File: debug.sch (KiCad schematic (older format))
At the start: 47 parts, among them J1 ZX62D-AB-5P8, P1 LPC-Link, P2 UART, P3 JTAG, P4 Cortex-Debug, P5 Vout, U1 93C46, U2 PRTR5V0U2X, U3 FT2232H, U4 LD1117S33CTR, X1 12MHz

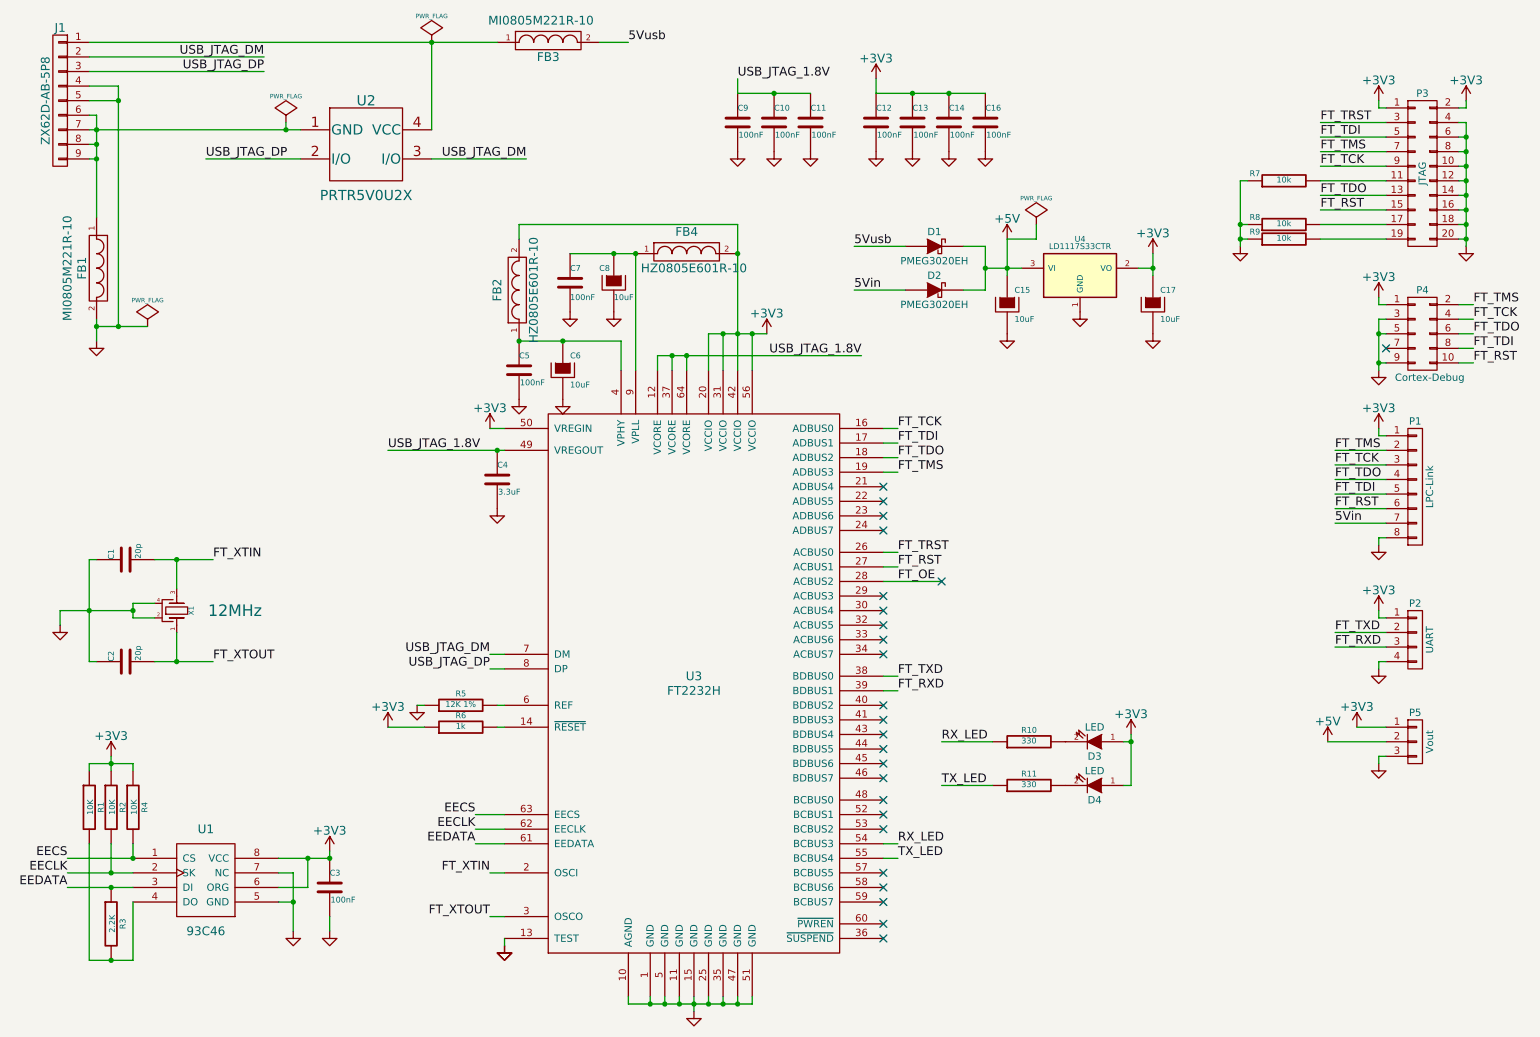
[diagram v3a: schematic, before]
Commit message: pcb terminado, enviado a fabricacion
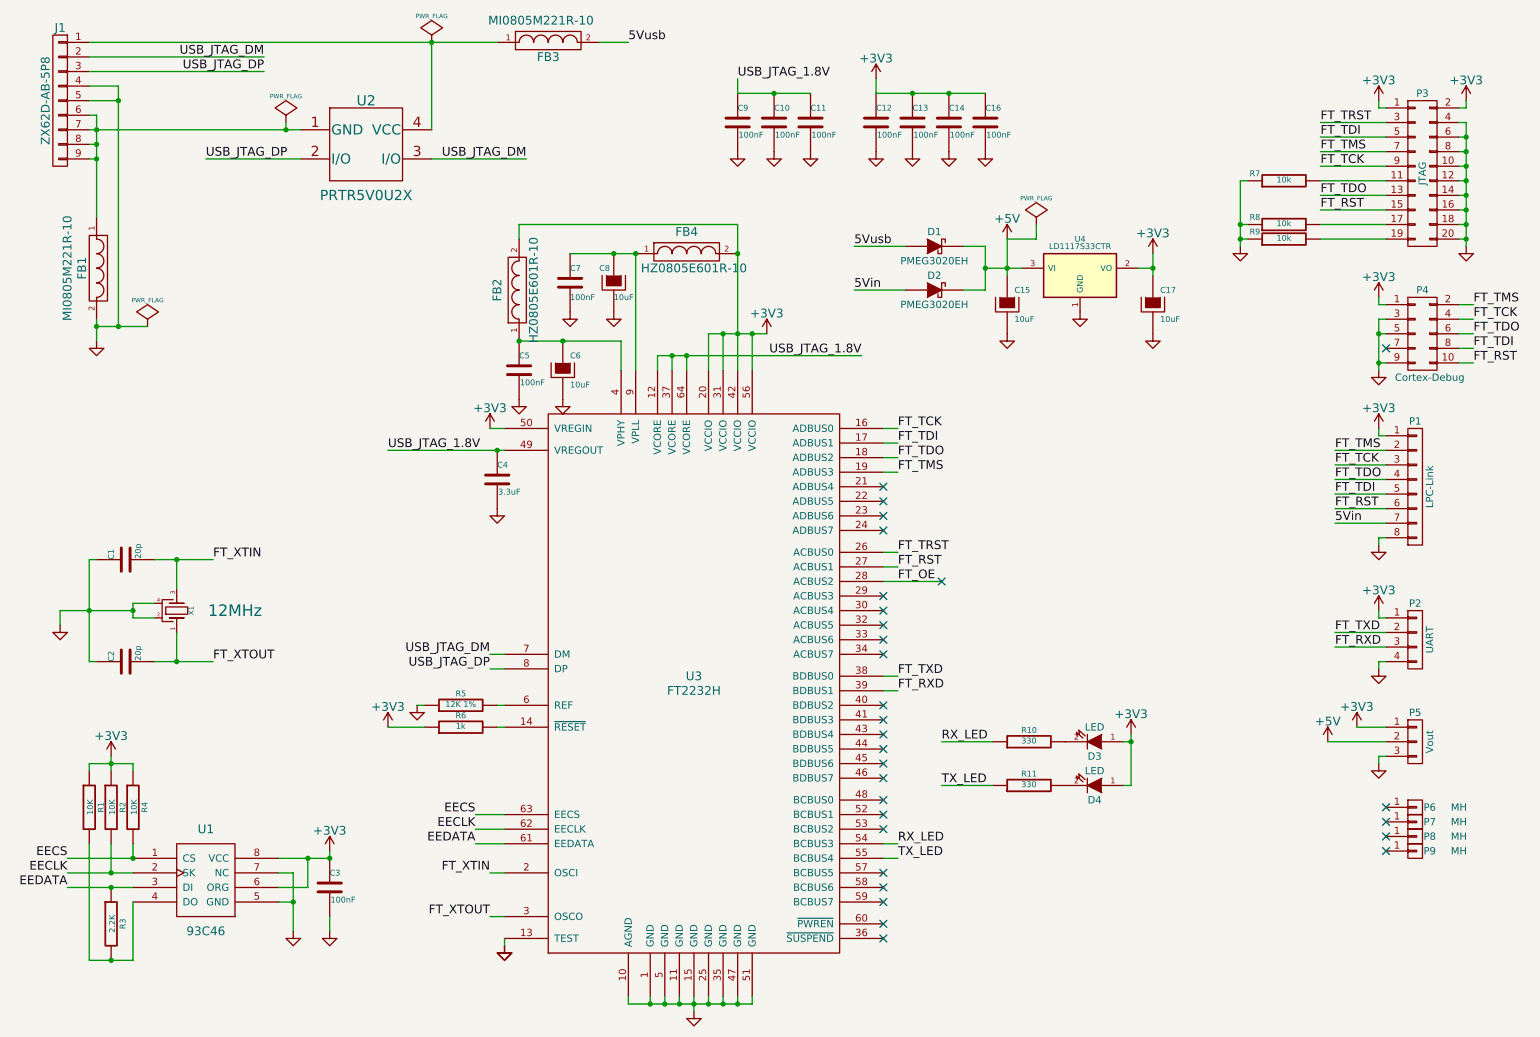
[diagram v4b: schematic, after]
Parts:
- added P6, P7, P8, P9: MH, Connect:1pin, symbol CONN_01X01
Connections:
- no-connect marks 25 -> 29
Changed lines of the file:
@@
 Connection ~ 1200 1350
 Wire Wire Line
-	1150 1350 1200 1350
-Wire Wire Line
-	1200 1350 2500 1350
-Wire Wire Line
-	2500 1350 2600 1350
-Wire Wire Line
-	1200 1250 1200 1350
-Wire Wire Line
-	1200 1350 1200 1450
-Wire Wire Line
-	1200 1450 1200 1550
-Wire Wire Line
-	1200 1550 1200 1950
+	1150 1350 2600 1350
+Wire Wire Line
+	1200 1250 1200 1950
 Wire Wire Line
 	1150 1250 1200 1250
@@
 	1150 1150 1350 1150
 Wire Wire Line
-	1200 2700 1350 2700
-Wire Wire Line
-	1350 2700 1550 2700
-Wire Wire Line
-	1150 750  3500 750
-Wire Wire Line
-	3500 750  3950 750
+	1200 2700 1550 2700
+Wire Wire Line
+	1150 750  3950 750
 Connection ~ 1200 2700
 Wire Wire Line
-	1350 1050 1350 1150
-Wire Wire Line
-	1350 1150 1350 2700
+	1350 1050 1350 2700
 Wire Wire Line
 	1150 950  2350 950
@@
 	3900 3400 4000 3400
 Wire Wire Line
-	5300 7300 5300 7350
-Wire Wire Line
-	5300 7350 5300 7400
-Wire Wire Line
-	1200 2650 1200 2700
-Wire Wire Line
-	1200 2700 1200 2800
+	5300 7300 5300 7400
+Wire Wire Line
+	1200 2650 1200 2800
 Connection ~ 3950 3550
 Connection ~ 5600 2200
@@
 Connection ~ 6800 1100
 Wire Wire Line
-	6550 1100 6800 1100
-Wire Wire Line
-	6800 1100 7050 1100
-Wire Wire Line
-	7050 1100 7300 1100
+	6550 1100 7300 1100
 Wire Wire Line
 	6550 1000 6550 1100
 Connection ~ 5850 1100
 Wire Wire Line
-	5600 1100 5850 1100
-Wire Wire Line
-	5850 1100 6100 1100
+	5600 1100 6100 1100
 Wire Wire Line
 	5600 1000 5600 1100
@@
 Connection ~ 4750 2200
 Wire Wire Line
-	4450 2200 4750 2200
-Wire Wire Line
-	4750 2200 4900 2200
+	4450 2200 4900 2200
 Wire Wire Line
 	4900 2200 4900 3000
 Connection ~ 5600 2750
 Wire Wire Line
-	5600 2000 5600 2200
-Wire Wire Line
-	5600 2200 5600 2750
-Wire Wire Line
-	5600 2750 5600 3000
+	5600 2000 5600 3000
 Connection ~ 5500 2750
 Wire Wire Line
@@
 	5700 2750 5700 3000
 Wire Wire Line
-	5400 2750 5500 2750
-Wire Wire Line
-	5500 2750 5600 2750
-Wire Wire Line
-	5600 2750 5700 2750
-Wire Wire Line
-	5700 2750 5800 2750
+	5400 2750 5800 2750
 Connection ~ 5250 2900
 Wire Wire Line
@@
 	5050 2900 5050 3000
 Wire Wire Line
-	5050 2900 5150 2900
-Wire Wire Line
-	5150 2900 5250 2900
-Wire Wire Line
-	5250 2900 6450 2900
+	5050 2900 6450 2900
 Connection ~ 4400 2800
 Wire Wire Line
 	4800 2800 4800 3000
 Wire Wire Line
-	4100 2800 4400 2800
-Wire Wire Line
-	4400 2800 4800 2800
-Wire Wire Line
-	3200 3550 3950 3550
-Wire Wire Line
-	3950 3550 4000 3550
+	4100 2800 4800 2800
+Wire Wire Line
+	3200 3550 4000 3550
 Wire Wire Line
 	4000 5050 3900 5050
@@
 	5700 7350 5700 7300
 Wire Wire Line
-	4850 7350 5000 7350
-Wire Wire Line
-	5000 7350 5100 7350
-Wire Wire Line
-	5100 7350 5200 7350
-Wire Wire Line
-	5200 7350 5300 7350
-Wire Wire Line
-	5300 7350 5400 7350
-Wire Wire Line
-	5400 7350 5500 7350
-Wire Wire Line
-	5500 7350 5600 7350
-Wire Wire Line
-	5600 7350 5700 7350
+	4850 7350 5700 7350
 Wire Wire Line
 	5000 7300 5000 7350
@@
 	1300 6450 1300 6250
 Wire Wire Line
-	1000 6450 1300 6450
-Wire Wire Line
-	1300 6450 1450 6450
+	1000 6450 1450 6450
 Wire Wire Line
 	1450 6350 1450 6250
@@
 Connection ~ 1300 5700
 Wire Wire Line
-	1150 5700 1300 5700
-Wire Wire Line
-	1300 5700 1450 5700
+	1150 5700 1450 5700
 Wire Wire Line
 	1150 5750 1150 5700
 Wire Wire Line
-	1300 5650 1300 5700
-Wire Wire Line
-	1300 5700 1300 5750
-Wire Wire Line
-	1000 6550 1300 6550
-Wire Wire Line
-	1300 6550 1450 6550
+	1300 5650 1300 5750
+Wire Wire Line
+	1000 6550 1450 6550
 Connection ~ 2800 6350
 Wire Wire Line
@@
 	2450 6550 2650 6550
 Wire Wire Line
-	2450 6350 2650 6350
-Wire Wire Line
-	2650 6350 2800 6350
+	2450 6350 2800 6350
 Connection ~ 2550 6650
 Wire Wire Line
@@
 	3900 6450 4000 6450
 Wire Wire Line
-	1600 4300 1750 4300
-Wire Wire Line
-	1750 4300 2000 4300
+	1600 4300 2000 4300
 Wire Wire Line
 	1200 4300 1150 4300
@@
 	1150 5000 1200 5000
 Wire Wire Line
-	1150 4300 1150 4650
-Wire Wire Line
-	1150 4650 1150 5000
+	1150 4300 1150 5000
 Connection ~ 1750 5000
 Connection ~ 1750 4300
 Wire Wire Line
-	1600 5000 1750 5000
-Wire Wire Line
-	1750 5000 2000 5000
+	1600 5000 2000 5000
 Wire Wire Line
 	10550 2950 10650 2950
@@
 	10050 2750 10000 2750
 Wire Wire Line
-	10000 2650 10000 2750
-Wire Wire Line
-	10000 2750 10000 2950
-Wire Wire Line
-	10000 2950 10000 3000
+	10000 2650 10000 3000
 Wire Wire Line
 	10050 2650 10000 2650
@@
 $EndComp
 Wire Wire Line
-	950  4650 1150 4650
-Wire Wire Line
-	1150 4650 1450 4650
+	950  4650 1450 4650
 Wire Wire Line
 	950  4650 950  4750
@@
 	1750 4800 1750 5000
 Wire Wire Line
-	1150 7050 1300 7050
-Wire Wire Line
-	1300 7050 1450 7050
+	1150 7050 1450 7050
 Wire Wire Line
 	1450 7050 1450 6650
@@
 $EndComp
 Wire Wire Line
-	10600 1300 10600 1400
-Wire Wire Line
-	10600 1400 10600 1500
-Wire Wire Line
-	10600 1500 10600 1600
-Wire Wire Line
-	10600 1600 10600 1700
-Wire Wire Line
-	10600 1700 10600 1800
-Wire Wire Line
-	10600 1800 10600 1900
-Wire Wire Line
-	10600 1900 10600 2000
-Wire Wire Line
-	10600 2000 10600 2100
-Wire Wire Line
-	10600 2100 10600 2150
+	10600 1300 10600 2150
 Wire Wire Line
 	10600 1300 10550 1300
@@
 $EndComp
 Wire Wire Line
-	8300 5500 8300 5550
-Wire Wire Line
-	8300 5550 8300 5850
+	8300 5500 8300 5850
 Wire Wire Line
 	8300 5850 8250 5850
@@
 $EndComp
 Wire Wire Line
-	9050 1700 9050 2000
-Wire Wire Line
-	9050 2000 9050 2100
-Wire Wire Line
-	9050 2100 9050 2150
+	9050 1700 9050 2150
 Wire Wire Line
 	9050 1700 9100 1700
@@
 $EndComp
 Wire Wire Line
-	7450 2100 7450 2300
-Wire Wire Line
-	7450 2300 7450 2350
-Wire Wire Line
-	7300 2300 7450 2300
-Wire Wire Line
-	7450 2300 7550 2300
+	7450 2100 7450 2350
+Wire Wire Line
+	7300 2300 7550 2300
 Connection ~ 7450 2300
 Wire Wire Line
 	8350 2300 8450 2300
 Wire Wire Line
-	8450 2200 8450 2300
-Wire Wire Line
-	8450 2300 8450 2350
+	8450 2200 8450 2350
 $Comp
 L +3V3 #PWR044
@@
 	1600 4600 1450 4600
 Wire Wire Line
-	1450 4600 1450 4650
-Wire Wire Line
-	1450 4650 1450 4700
+	1450 4600 1450 4700
 Wire Wire Line
 	1450 4700 1600 4700
@@
 	7150 2150 7300 2150
 Wire Wire Line
-	7300 2150 7300 2300
-Wire Wire Line
-	7300 2300 7300 2450
+	7300 2150 7300 2450
 Wire Wire Line
 	7300 2450 7150 2450
@@
 	2450 6450 2550 6450
 Wire Wire Line
-	2550 6450 2550 6650
-Wire Wire Line
-	2550 6650 2550 6850
+	2550 6450 2550 6850
 $Comp
 L PWR_FLAG #FLG045
@@
 	2500 1300 2500 1350
 Connection ~ 2500 1350
+$Comp
+L CONN_01X01 P6
+U 1 1 55E0C75E
+P 10250 6000
+F 0 "P6" H 10350 6000 50  0000 C CNN
+F 1 "MH" H 10550 6000 50  0000 C CNN
+F 2 "Connect:1pin" H 10250 6000 60  0001 C CNN
+F 3 "" H 10250 6000 60  0000 C CNN
+	1    10250 6000
+	1    0    0    -1
+$EndComp
+$Comp
+L CONN_01X01 P7
+U 1 1 55E0D225
+P 10250 6100
+F 0 "P7" H 10350 6100 50  0000 C CNN
+F 1 "MH" H 10550 6100 50  0000 C CNN
+F 2 "Connect:1pin" H 10250 6100 60  0001 C CNN
+F 3 "" H 10250 6100 60  0000 C CNN
+	1    10250 6100
+	1    0    0    -1
+$EndComp
+$Comp
+L CONN_01X01 P8
+U 1 1 55E0D26E
+P 10250 6200
+F 0 "P8" H 10350 6200 50  0000 C CNN
+F 1 "MH" H 10550 6200 50  0000 C CNN
+F 2 "Connect:1pin" H 10250 6200 60  0001 C CNN
+F 3 "" H 10250 6200 60  0000 C CNN
+	1    10250 6200
+	1    0    0    -1
+$EndComp
+$Comp
+L CONN_01X01 P9
+U 1 1 55E0D2B4
+P 10250 6300
+F 0 "P9" H 10350 6300 50  0000 C CNN
+F 1 "MH" H 10550 6300 50  0000 C CNN
+F 2 "Connect:1pin" H 10250 6300 60  0001 C CNN
+F 3 "" H 10250 6300 60  0000 C CNN
+	1    10250 6300
+	1    0    0    -1
+$EndComp
+NoConn ~ 10050 6000
+NoConn ~ 10050 6100
+NoConn ~ 10050 6200
+NoConn ~ 10050 6300
 $EndSCHEMATC
